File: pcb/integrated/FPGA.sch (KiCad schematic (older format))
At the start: 28 parts, among them J3001 Conn_01x04_Male, J3002 Conn_01x06_Male, U3001 XC7S25-L1FTGB196, U3002 S25FL127SABN, U3003 74AVC4TD245BQ

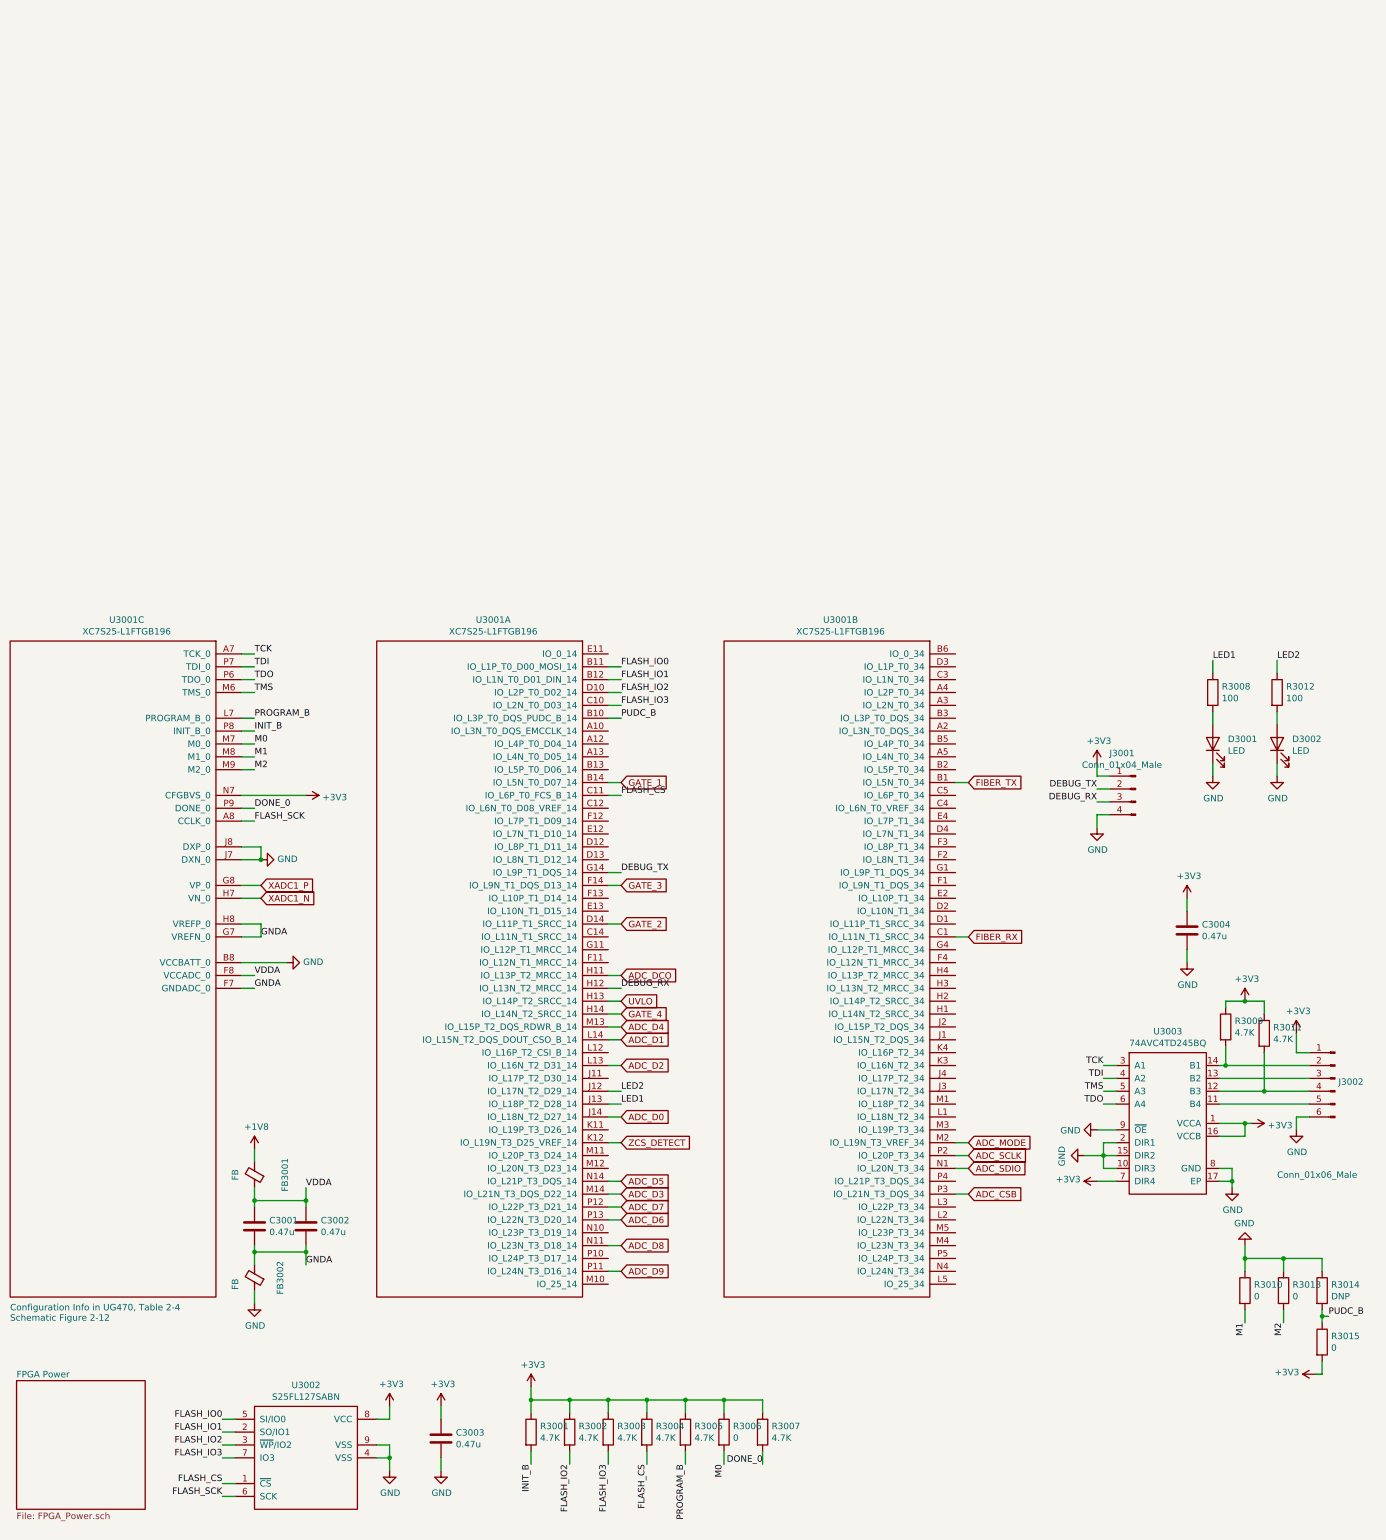
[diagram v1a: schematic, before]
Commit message: routing, all componens placed on PCB
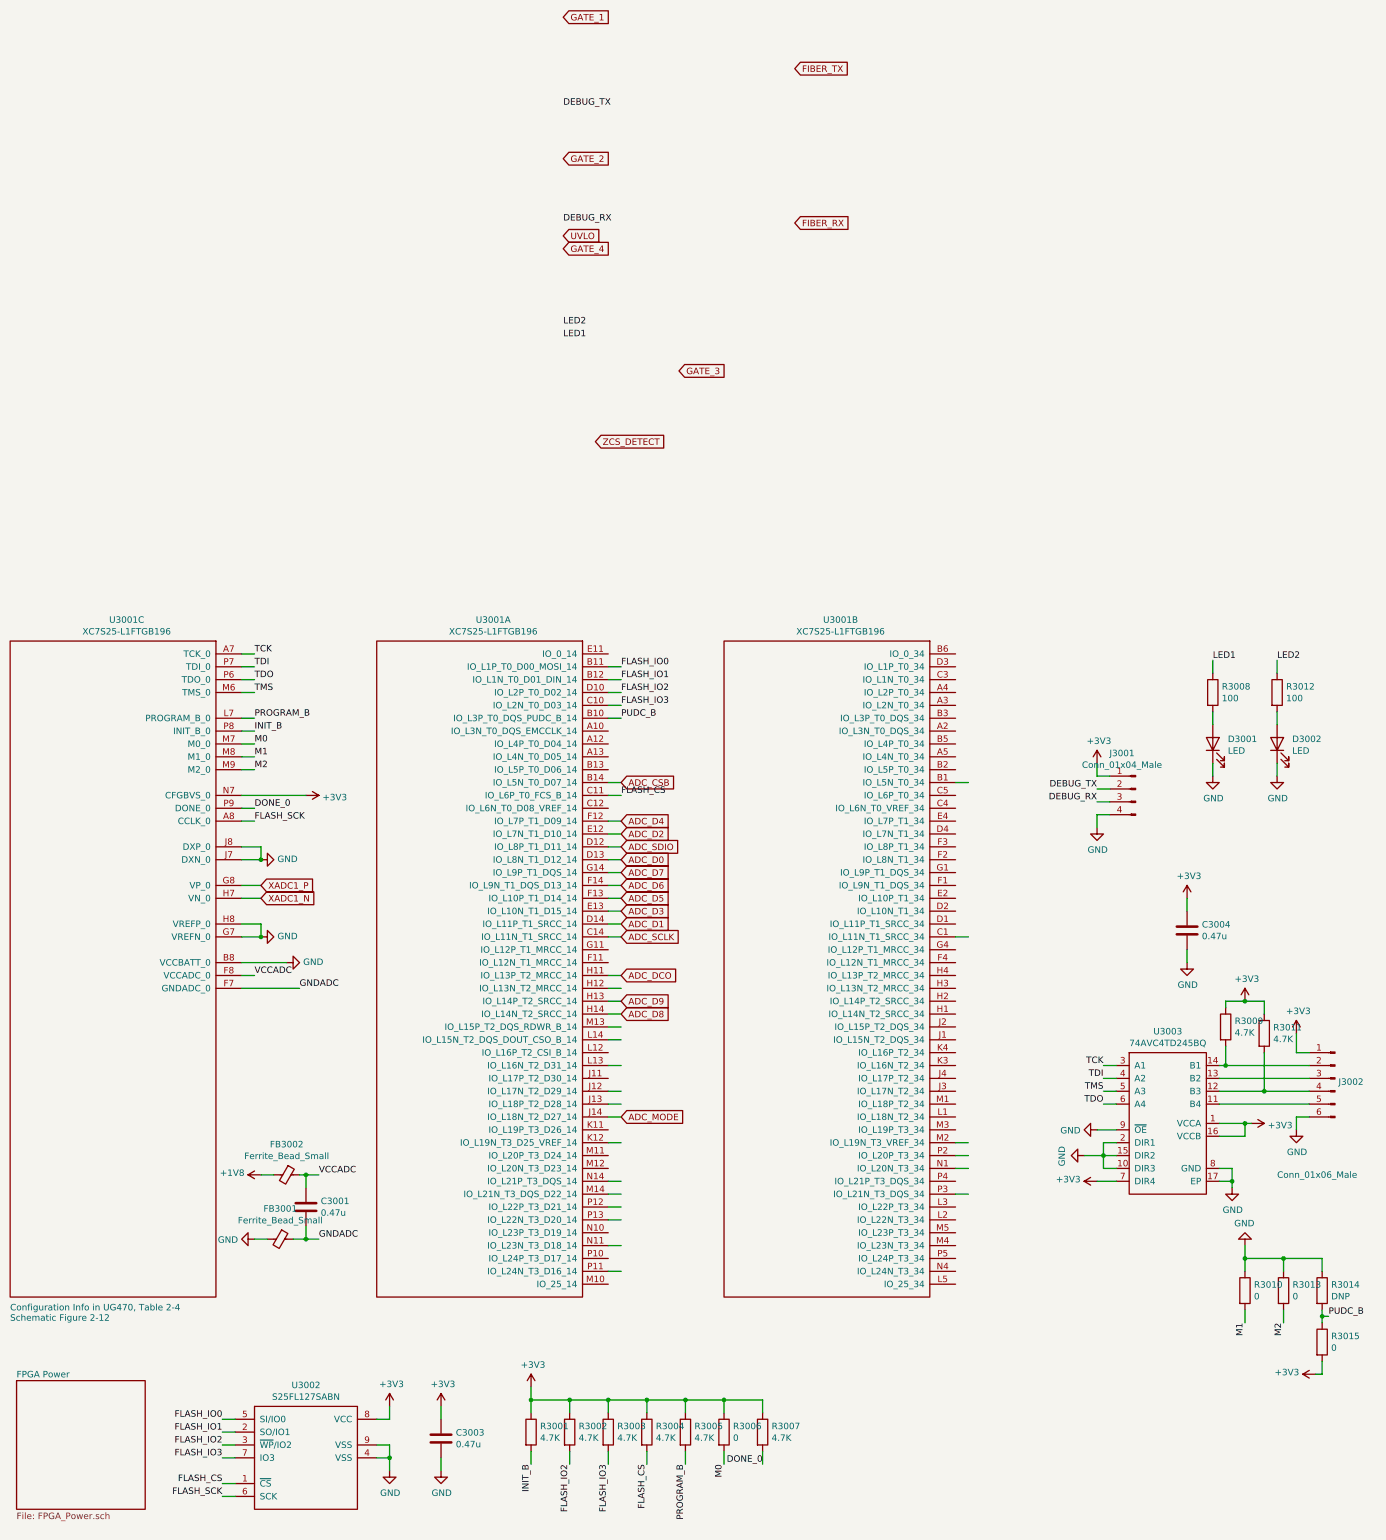
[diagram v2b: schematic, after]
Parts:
- removed C3002: 0.47u, Capacitor_SMD:C_0402_1005Metric, symbol Device:C
- D3001, D3002: footprint wbraun_smd:LED-T1-RIGHT-ANGLE_4.6x4.4mm -> LED_SMD:LED_0805_2012Metric
- FB3001, FB3002: value FB -> Ferrite_Bead_Small; footprint Inductor_SMD:L_0805_2012Metric -> Inductor_SMD:L_0402_1005Metric
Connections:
- net labels added: GNDADC, VCCADC
- net labels removed: GNDA, VDDA
- wire segments 166 -> 169
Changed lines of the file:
@@
 Text Notes 650  6050 0    50   ~ 0
 Configuration Info in UG470, Table 2-4\nSchematic Figure 2-12\n
-$Comp
-L power:GND #PWR03001
-U 1 1 5C05B0BC
-P 2550 5900
-F 0 "#PWR03001" H 2550 5650 50  0001 C CNN
-F 1 "GND" H 2555 5727 50  0000 C CNN
-F 2 "" H 2550 5900 50  0001 C CNN
-F 3 "" H 2550 5900 50  0001 C CNN
-	1    2550 5900
-	1    0    0    -1
-$EndComp
 Wire Wire Line
 	2450 2950 2600 2950
@@
 Wire Wire Line
 	5300 5450 5400 5450
-Text GLabel 5400 5650 2    50   Input ~ 0
+Text GLabel 5400 3550 2    50   Input ~ 0
 ADC_D9
-Text GLabel 5400 5450 2    50   Input ~ 0
+Text GLabel 5400 3650 2    50   Input ~ 0
 ADC_D8
-Text GLabel 5400 5150 2    50   Input ~ 0
+Text GLabel 5400 2550 2    50   Input ~ 0
 ADC_D7
-Text GLabel 5400 5250 2    50   Input ~ 0
+Text GLabel 5400 2650 2    50   Input ~ 0
 ADC_D6
-Text GLabel 5400 4950 2    50   Input ~ 0
+Text GLabel 5400 2750 2    50   Input ~ 0
 ADC_D5
-Text GLabel 5400 3750 2    50   Input ~ 0
+Text GLabel 5400 2150 2    50   Input ~ 0
 ADC_D4
-Text GLabel 5400 5050 2    50   Input ~ 0
+Text GLabel 5400 2850 2    50   Input ~ 0
 ADC_D3
-Text GLabel 5400 4050 2    50   Input ~ 0
+Text GLabel 5400 2250 2    50   Input ~ 0
 ADC_D2
-Text GLabel 5400 3850 2    50   Input ~ 0
+Text GLabel 5400 2950 2    50   Input ~ 0
 ADC_D1
-Text GLabel 5400 4450 2    50   Input ~ 0
+Text GLabel 5400 2450 2    50   Input ~ 0
 ADC_D0
 Wire Wire Line
@@
 F 0 "D3002" V 10538 1433 50  0000 R CNN
 F 1 "LED" V 10447 1433 50  0000 R CNN
-F 2 "wbraun_smd:LED-T1-RIGHT-ANGLE_4.6x4.4mm" H 10500 1550 50  0001 C CNN
+F 2 "LED_SMD:LED_0805_2012Metric" H 10500 1550 50  0001 C CNN
 F 3 "~" H 10500 1550 50  0001 C CNN
 	1    10500 1550
@@
 F 0 "D3001" V 10038 1433 50  0000 R CNN
 F 1 "LED" V 9947 1433 50  0000 R CNN
-F 2 "wbraun_smd:LED-T1-RIGHT-ANGLE_4.6x4.4mm" H 10000 1550 50  0001 C CNN
+F 2 "LED_SMD:LED_0805_2012Metric" H 10000 1550 50  0001 C CNN
 F 3 "~" H 10000 1550 50  0001 C CNN
 	1    10000 1550
@@
 Wire Wire Line
 	5300 1850 5400 1850
-Text GLabel 5400 1850 2    50   Input ~ 0
+Text GLabel 4950 -4100 2    50   Input ~ 0
 GATE_1
 Wire Wire Line
 	5300 2950 5400 2950
-Text GLabel 5400 2950 2    50   Input ~ 0
+Text GLabel 4950 -3000 2    50   Input ~ 0
 GATE_2
 Wire Wire Line
 	5300 2650 5400 2650
-Text GLabel 5400 2650 2    50   Input ~ 0
+Text GLabel 5850 -1350 2    50   Input ~ 0
 GATE_3
 Wire Wire Line
 	5300 3650 5400 3650
-Text GLabel 5400 3650 2    50   Input ~ 0
+Text GLabel 4950 -2300 2    50   Input ~ 0
 GATE_4
 Wire Wire Line
@@
 Wire Wire Line
 	8000 1850 8100 1850
-Text GLabel 8100 1850 2    50   Input ~ 0
+Text GLabel 6750 -3700 2    50   Input ~ 0
 FIBER_TX
-Text GLabel 8100 3050 2    50   Input ~ 0
+Text GLabel 6750 -2500 2    50   Input ~ 0
 FIBER_RX
 Wire Wire Line
@@
 Wire Wire Line
 	5300 3550 5400 3550
-Text GLabel 5400 4650 2    50   Input ~ 0
+Text GLabel 5200 -800 2    50   Input ~ 0
 ZCS_DETECT
 Wire Wire Line
 	8000 5050 8100 5050
-Text GLabel 8100 5050 2    50   Input ~ 0
+Text GLabel 5400 1850 2    50   Input ~ 0
 ADC_CSB
 Wire Wire Line
 	8000 4750 8100 4750
-Text GLabel 8100 4750 2    50   Input ~ 0
+Text GLabel 5400 3050 2    50   Input ~ 0
 ADC_SCLK
-Text GLabel 8100 4850 2    50   Input ~ 0
+Text GLabel 5400 2350 2    50   Input ~ 0
 ADC_SDIO
-Text GLabel 8100 4650 2    50   Input ~ 0
+Text GLabel 5400 4450 2    50   Input ~ 0
 ADC_MODE
 Wire Wire Line
 	5300 4650 5400 4650
-Text GLabel 5400 3550 2    50   Input ~ 0
+Text GLabel 4950 -2400 2    50   Input ~ 0
 UVLO
 Wire Wire Line
 	5300 3450 5400 3450
-Text Label 5400 3450 0    50   ~ 0
+Text Label 4950 -2500 0    50   ~ 0
 DEBUG_RX
 Wire Wire Line
 	5300 2550 5400 2550
-Text Label 5400 2550 0    50   ~ 0
+Text Label 4950 -3400 0    50   ~ 0
 DEBUG_TX
 Wire Wire Line
 	5300 4350 5400 4350
-Text Label 5400 4350 0    50   ~ 0
+Text Label 4950 -1600 0    50   ~ 0
 LED1
 Wire Wire Line
 	5300 4250 5400 4250
-Text Label 5400 4250 0    50   ~ 0
+Text Label 4950 -1700 0    50   ~ 0
 LED2
 $Comp
@@
 Wire Wire Line
 	10100 3550 10250 3550
-$Comp
-L Device:Ferrite_Bead_Small FB3002
-U 1 1 5D870ADB
-P 2550 5700
-F 0 "FB3002" V 2350 5700 50  0000 C CNN
-F 1 "FB" V 2700 5750 50  0000 C CNN
-F 2 "Inductor_SMD:L_0805_2012Metric" V 2480 5700 50  0001 C CNN
-F 3 "~" H 2550 5700 50  0001 C CNN
-	1    2550 5700
-	-1   0    0    1
-$EndComp
-$Comp
-L Device:Ferrite_Bead_Small FB3001
-U 1 1 5D877083
-P 2550 4900
-F 0 "FB3001" V 2313 4900 50  0000 C CNN
-F 1 "FB" V 2700 4900 50  0000 C CNN
-F 2 "Inductor_SMD:L_0805_2012Metric" V 2480 4900 50  0001 C CNN
-F 3 "~" H 2550 4900 50  0001 C CNN
-	1    2550 4900
-	-1   0    0    1
-$EndComp
-$Comp
-L Device:C C3001
-U 1 1 5D8773FD
-P 2550 5300
-F 0 "C3001" H 2665 5346 50  0000 L CNN
-F 1 "0.47u" H 2665 5255 50  0000 L CNN
-F 2 "Capacitor_SMD:C_0402_1005Metric" H 2588 5150 50  0001 C CNN
-F 3 "~" H 2550 5300 50  0001 C CNN
-	1    2550 5300
-	1    0    0    -1
-$EndComp
-$Comp
-L Device:C C3002
-U 1 1 5D877505
-P 2950 5300
-F 0 "C3002" H 3065 5346 50  0000 L CNN
-F 1 "0.47u" H 3065 5255 50  0000 L CNN
-F 2 "Capacitor_SMD:C_0402_1005Metric" H 2988 5150 50  0001 C CNN
-F 3 "~" H 2950 5300 50  0001 C CNN
-	1    2950 5300
-	1    0    0    -1
-$EndComp
-Wire Wire Line
-	2550 5000 2550 5100
-Wire Wire Line
-	2550 5100 2950 5100
-Wire Wire Line
-	2950 5100 2950 5150
-Connection ~ 2550 5100
-Wire Wire Line
-	2550 5100 2550 5150
-Wire Wire Line
-	2550 5450 2550 5500
-Wire Wire Line
-	2550 5500 2950 5500
-Wire Wire Line
-	2950 5500 2950 5450
-Wire Wire Line
-	2550 5500 2550 5600
-Connection ~ 2550 5500
-Wire Wire Line
-	2550 4800 2550 4700
-Wire Wire Line
-	2550 5800 2550 5900
-Wire Wire Line
-	2950 5100 2950 5000
-Connection ~ 2950 5100
-Wire Wire Line
-	2950 5500 2950 5600
-Connection ~ 2950 5500
-Text Label 2950 5600 0    50   ~ 0
-GNDA
-Text Label 2950 5000 0    50   ~ 0
-VDDA
-Text Label 2550 3450 0    50   ~ 0
-GNDA
-Text Label 2550 3350 0    50   ~ 0
-VDDA
 Wire Wire Line
 	2450 3350 2550 3350
-Wire Wire Line
-	2450 3450 2550 3450
 $Comp
 L power:GND #PWR03003
@@
 Wire Wire Line
 	2450 3250 2800 3250
-Text Label 2600 3050 0    50   ~ 0
-GNDA
 $Comp
 L power:GND #PWR03002
@@
 $EndComp
 $Comp
-L power:+1V8 #PWR0163
-U 1 1 5D7E8C3A
-P 2550 4700
-F 0 "#PWR0163" H 2550 4550 50  0001 C CNN
-F 1 "+1V8" H 2565 4873 50  0000 C CNN
-F 2 "" H 2550 4700 50  0001 C CNN
-F 3 "" H 2550 4700 50  0001 C CNN
-	1    2550 4700
-	1    0    0    -1
-$EndComp
-$Comp
 L power:+3V3 #PWR0164
 U 1 1 5D7E9482
@@
 	0    1    1    0
 $EndComp
+$Comp
+L power:GND #PWR0163
+U 1 1 5DE28CC2
+P 2600 3050
+F 0 "#PWR0163" H 2600 2800 50  0001 C CNN
+F 1 "GND" V 2605 2922 50  0000 R CNN
+F 2 "" H 2600 3050 50  0001 C CNN
+F 3 "" H 2600 3050 50  0001 C CNN
+	1    2600 3050
+	0    -1   -1   0
+$EndComp
+Connection ~ 2600 3050
+$Comp
+L power:+1V8 #PWR0194
+U 1 1 5DE2A2AA
+P 2600 4900
+F 0 "#PWR0194" H 2600 4750 50  0001 C CNN
+F 1 "+1V8" V 2615 5028 50  0000 L CNN
+F 2 "" H 2600 4900 50  0001 C CNN
+F 3 "" H 2600 4900 50  0001 C CNN
+	1    2600 4900
+	0    -1   -1   0
+$EndComp
+Wire Wire Line
+	2450 3450 2900 3450
+$Comp
+L power:GND #PWR0195
+U 1 1 5DF37C1F
+P 2550 5400
+F 0 "#PWR0195" H 2550 5150 50  0001 C CNN
+F 1 "GND" V 2555 5272 50  0000 R CNN
+F 2 "" H 2550 5400 50  0001 C CNN
+F 3 "" H 2550 5400 50  0001 C CNN
+	1    2550 5400
+	0    1    1    0
+$EndComp
+Wire Wire Line
+	2600 4900 2700 4900
+Wire Wire Line
+	2550 5400 2650 5400
+Wire Wire Line
+	2850 5400 2950 5400
+Wire Wire Line
+	2950 5400 2950 5300
+Wire Wire Line
+	2900 4900 2950 4900
+Wire Wire Line
+	2950 4900 2950 5000
+Wire Wire Line
+	2950 4900 3050 4900
+Connection ~ 2950 4900
+Wire Wire Line
+	2950 5400 3050 5400
+Connection ~ 2950 5400
+Text Label 3050 4900 0    50   ~ 0
+VCCADC
+Text Label 3050 5400 0    50   ~ 0
+GNDADC
+$Comp
+L Device:C C3001
+U 1 1 5DF382D1
+P 2950 5150
+F 0 "C3001" H 3065 5196 50  0000 L CNN
+F 1 "0.47u" H 3065 5105 50  0000 L CNN
+F 2 "Capacitor_SMD:C_0402_1005Metric" H 2988 5000 50  0001 C CNN
+F 3 "~" H 2950 5150 50  0001 C CNN
+	1    2950 5150
+	1    0    0    -1
+$EndComp
+Text Label 2550 3350 0    50   ~ 0
+VCCADC
+Text Label 2900 3450 0    50   ~ 0
+GNDADC
+$Comp
+L Device:Ferrite_Bead_Small FB3002
+U 1 1 5DF353BA
+P 2800 4900
+F 0 "FB3002" V 2563 4900 50  0000 C CNN
+F 1 "Ferrite_Bead_Small" V 2654 4900 50  0000 C CNN
+F 2 "Inductor_SMD:L_0402_1005Metric" V 2730 4900 50  0001 C CNN
+F 3 "~" H 2800 4900 50  0001 C CNN
+	1    2800 4900
+	0    1    1    0
+$EndComp
+$Comp
+L Device:Ferrite_Bead_Small FB3001
+U 1 1 5DF719D1
+P 2750 5400
+F 0 "FB3001" V 2513 5400 50  0000 C CNN
+F 1 "Ferrite_Bead_Small" V 2604 5400 50  0000 C CNN
+F 2 "Inductor_SMD:L_0402_1005Metric" V 2680 5400 50  0001 C CNN
+F 3 "~" H 2750 5400 50  0001 C CNN
+	1    2750 5400
+	0    1    1    0
+$EndComp
+Wire Wire Line
+	5300 2750 5400 2750
+Wire Wire Line
+	5300 2150 5400 2150
+Wire Wire Line
+	5300 2850 5400 2850
+Wire Wire Line
+	5300 2250 5400 2250
+Wire Wire Line
+	5300 2450 5400 2450
+Wire Wire Line
+	5300 2350 5400 2350
+Wire Wire Line
+	5300 3050 5400 3050
 $EndSCHEMATC
